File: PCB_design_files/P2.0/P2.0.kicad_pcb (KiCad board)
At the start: 4 copper layers, 19.8 x 10.9 mm, 31 parts, among them U1 INA819IDRGR

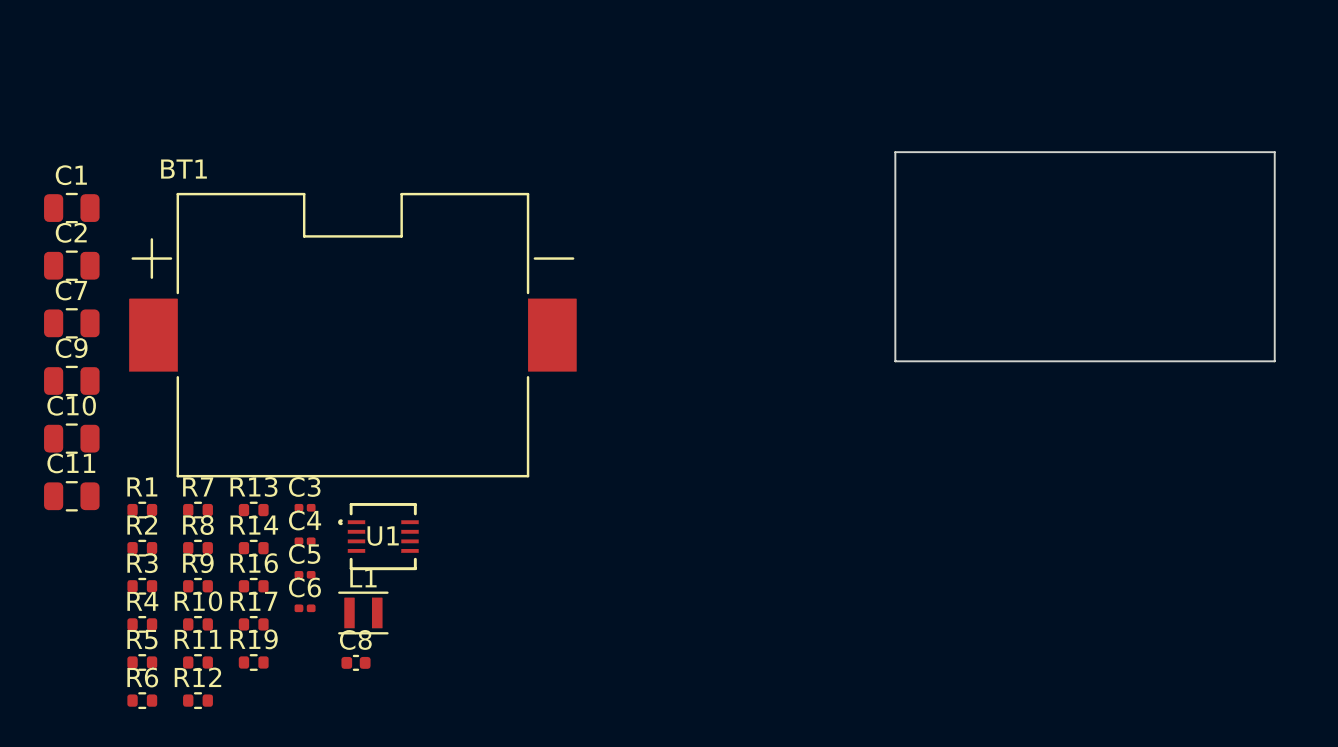
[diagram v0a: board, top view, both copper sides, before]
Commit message: PCB layout and component footprint updates
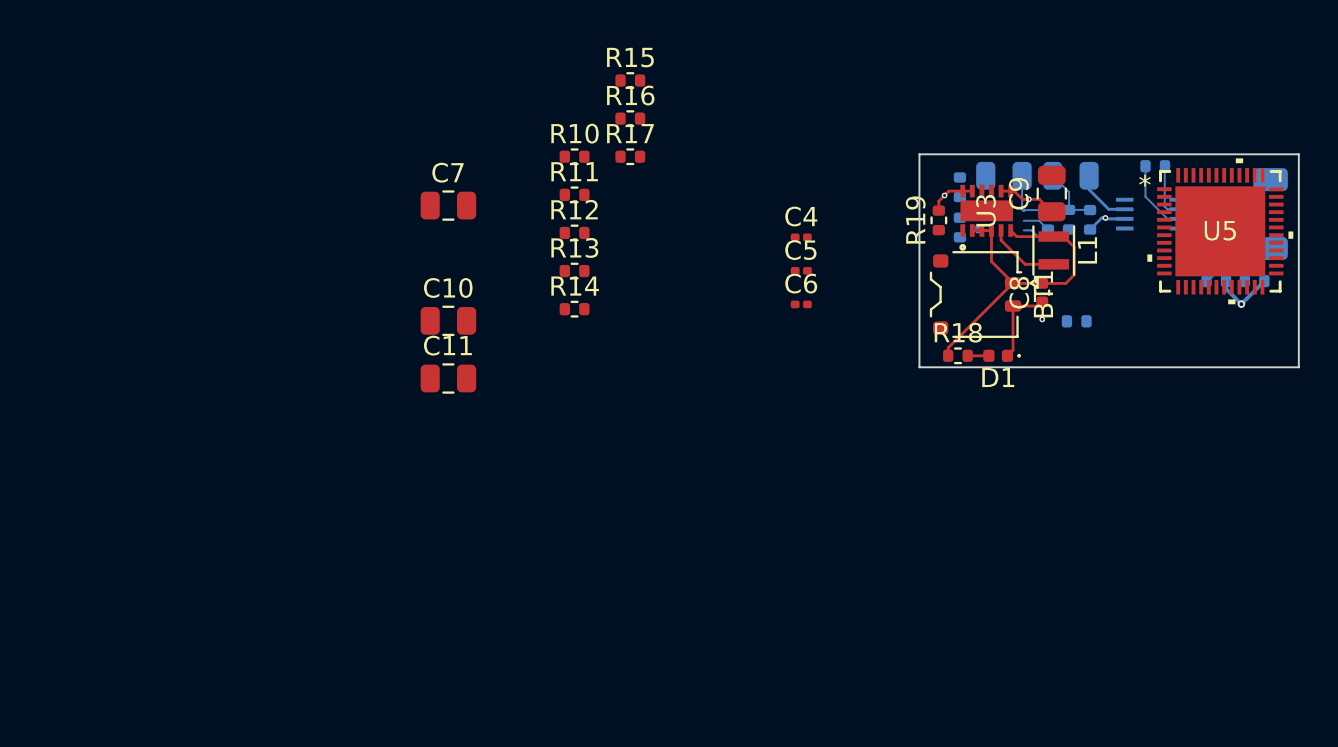
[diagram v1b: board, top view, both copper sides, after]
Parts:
- added D1: LED, LED_SMD:LED_0402_1005Metric, F.Cu at (80.3, 43.4)
- added J1: Conn_01x02_Pin, Connector_JST:JST_SH_BM02B-SRSS-TB_1x02-1MP_P1.00mm_Vertical, B.Cu at (93.3, 36.0)
- added R15: 100k, Resistor_SMD:R_0402_1005Metric, F.Cu at (61.1, 29.0)
- added R18: 1.1k, Resistor_SMD:R_0402_1005Metric, F.Cu at (78.2, 43.4)
- added U3: TPS61094, Library:TPS61094DSSR, F.Cu at (79.7, 35.8)
- added U5: NRF52832-QFAA-R, Library:QFN-48_NOR, F.Cu at (91.9, 36.9)
- BT1: footprint BHSD-1225-SM:BAT_BHSD-1225-SM -> Connector_JST:JST_ACH_BM02B-ACHSS-GAN-ETF_1x02-1MP_P1.20mm_Vertical
- C1, C2, C3, R1, R2, R3, R4, R5, R6, R7, R8, R9, U1: moved to B.Cu
- moved R1 59.3 mm to (93.7, 39.5)
- moved R2 57.8 mm to (91.7, 39.5)
- moved R3 57.3 mm to (88.5, 33.5), turned to 180 degrees
- moved R4 53.8 mm to (85.1, 36.3), turned to -90 degrees
- moved R5 53.6 mm to (84.0, 36.3), turned to -90 degrees
- moved R6 53.5 mm to (82.9, 36.3), turned to -90 degrees
- moved C1 52.2 mm to (84.1, 34.0), turned to 180 degrees
- moved C9 52.1 mm to (83.1, 34.9), turned to 90 degrees
- moved C2 48.9 mm to (80.6, 34.0), turned to 180 degrees
- moved R7 46.9 mm to (84.4, 41.6), turned to 180 degrees
- moved R9 44.9 mm to (78.3, 34.6), turned to -90 degrees
- moved U1 43.5 mm to (88.3, 36.0), turned to 180 degrees
- moved R8 43.2 mm to (78.3, 36.7), turned to -90 degrees
- moved R19 42.6 mm to (77.2, 36.3), turned to 90 degrees
- moved C8 40.7 mm to (82.6, 40.1), turned to 90 degrees
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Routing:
- net Net-(BT1-+): track 0.00 -> 17.9 mm
- net GND: track 0.00 -> 16.1 mm, vias 0 -> 5
- net /EEG+: track 0.00 -> 7.63 mm
- net /EEG-: track 0.00 -> 7.06 mm
- net Net-(R3-Pad2): track 0.00 -> 3.79 mm
- net Net-(U3-SW): track 0.00 -> 3.78 mm
- net Net-(C1-Pad2): track 0.00 -> 3.24 mm
- net Net-(U2-OUT1): track 0.00 -> 3.17 mm
- net Net-(U1-OUT): track 0.00 -> 3.01 mm
- net Net-(R3-Pad1): track 0.00 -> 2.88 mm
- net Net-(U2-IN1+): track 0.00 -> 2.78 mm
- net Net-(U2-IN1-): track 0.00 -> 1.45 mm
- net Net-(D1-A): track 0.00 -> 1.11 mm
- added copper zone on In2.Cu, net +3V3
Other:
- board size 19.8 x 10.9 mm -> 19.8 x 11.1 mm

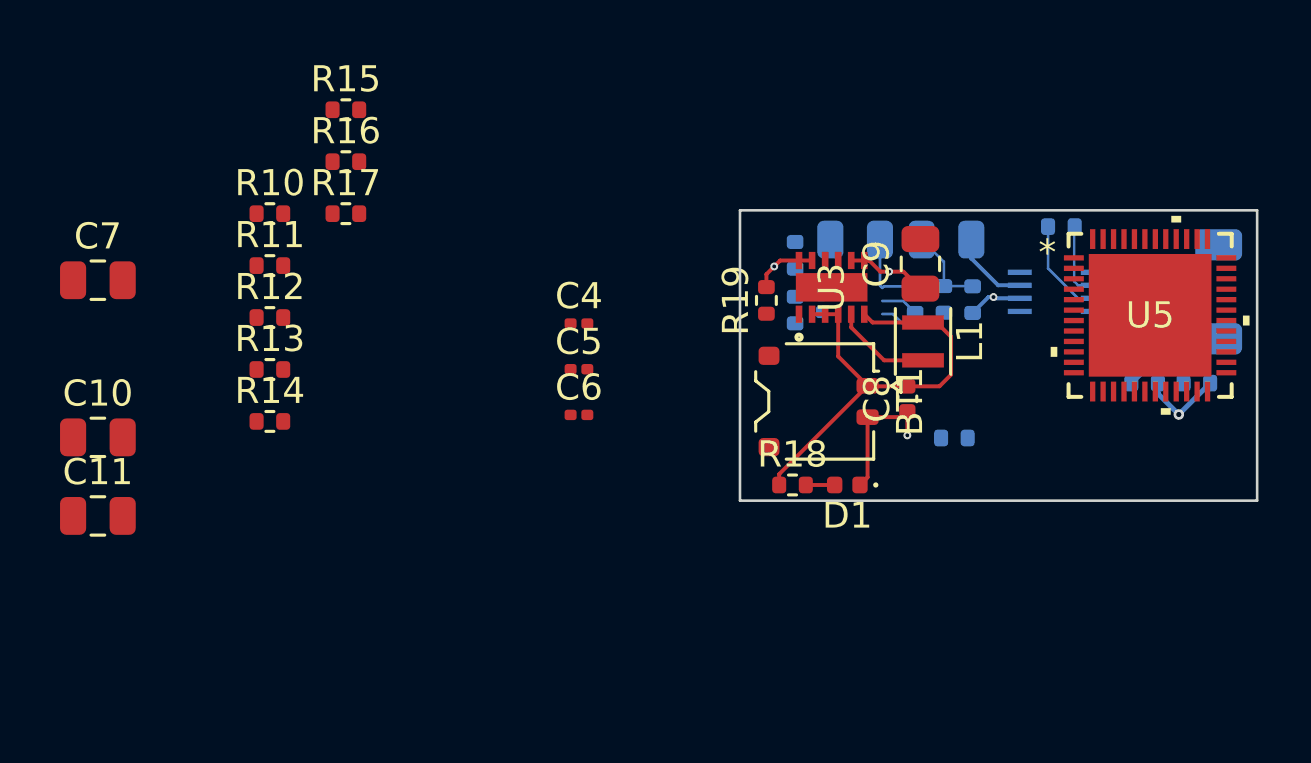
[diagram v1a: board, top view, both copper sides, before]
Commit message: Increased board size
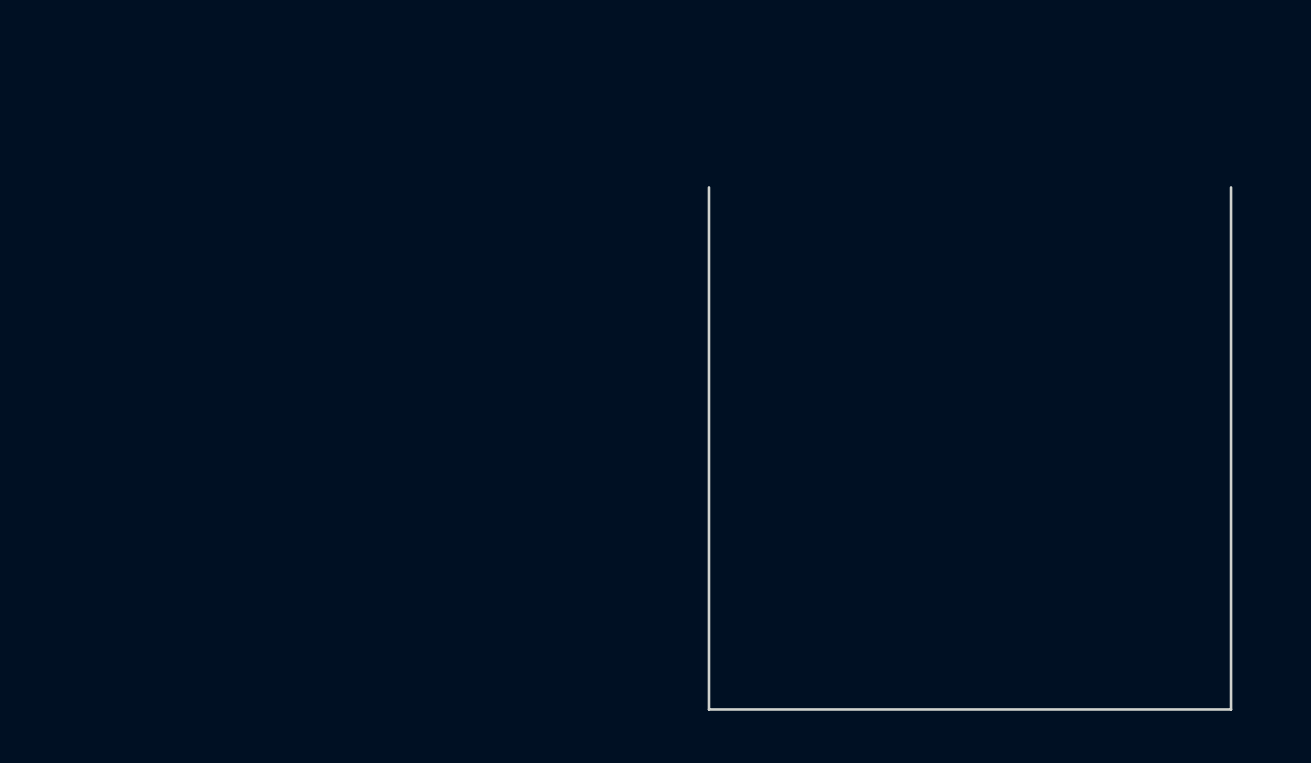
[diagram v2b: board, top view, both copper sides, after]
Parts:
- removed BT1: BHSD-1225-SM, Connector_JST:JST_ACH_BM02B-ACHSS-GAN-ETF_1x02-1MP_P1.20mm_Vertical
- removed C1, C10, C11, C2, C7: 10uF, Capacitor_SMD:C_0805_2012Metric
- removed C3, C4, C5: 0.1uF, Capacitor_SMD:C_0201_0603Metric
- removed C6: 10nF, Capacitor_SMD:C_0201_0603Metric
- removed C8: 2.2uF, Capacitor_SMD:C_0402_1005Metric
- removed C9: 33uF, Capacitor_SMD:C_0805_2012Metric
- removed D1: LED, LED_SMD:LED_0402_1005Metric
- removed J1: Conn_01x02_Pin, Connector_JST:JST_SH_BM02B-SRSS-TB_1x02-1MP_P1.00mm_Vertical
- removed L1: 2.2uH, Inductor_SMD:L_Murata_DFE201610P
- removed R1, R2: 68k, Resistor_SMD:R_0402_1005Metric
- removed R10: 604, Resistor_SMD:R_0402_1005Metric
- removed R11: 16k, Resistor_SMD:R_0402_1005Metric
- removed R12: 2.49k, Resistor_SMD:R_0402_1005Metric
- removed R13: 49.9k, Resistor_SMD:R_0402_1005Metric
- removed R14: 10k, Resistor_SMD:R_0402_1005Metric
- removed R15, R16, R4, R8, R9: 100k, Resistor_SMD:R_0402_1005Metric
- removed R17: ?150k, Resistor_SMD:R_0402_1005Metric
- removed R18, R19: 1.1k, Resistor_SMD:R_0402_1005Metric
- removed R3: 8.2k, Resistor_SMD:R_0402_1005Metric
- removed R5, R7: 1k, Resistor_SMD:R_0402_1005Metric
- removed R6: ?100k, Resistor_SMD:R_0402_1005Metric
- removed U1: INA819IDRGR, Library:SON_9IDRGR_TEX
- removed U3: TPS61094, Library:TPS61094DSSR
- removed U5: NRF52832-QFAA-R, Library:QFN-48_NOR
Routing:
- net Net-(BT1-+): track 17.9 -> 0.00 mm
- net GND: track 16.1 -> 0.00 mm, vias 5 -> 0
- net /EEG+: track 7.63 -> 0.00 mm
- net /EEG-: track 7.06 -> 0.00 mm
- net Net-(R3-Pad2): track 3.79 -> 0.00 mm
- net Net-(U3-SW): track 3.78 -> 0.00 mm
- net Net-(C1-Pad2): track 3.24 -> 0.00 mm
- net Net-(U2-OUT1): track 3.17 -> 0.00 mm
- net Net-(U1-OUT): track 3.01 -> 0.00 mm
- net Net-(R3-Pad1): track 2.88 -> 0.00 mm
- net Net-(U2-IN1+): track 2.78 -> 0.00 mm
- net Net-(U2-IN1-): track 1.45 -> 0.00 mm
- net Net-(D1-A): track 1.11 -> 0.00 mm
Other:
- board size 19.8 x 11.1 mm -> 20 x 20 mm

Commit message: Updated P2.0
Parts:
- added AE1: Antenna_Chip, Library:XDCR_2450AT18B100E, F.Cu at (76.2, 34.5)
- added BT1: BHSD-1225-SM, Connector_JST:JST_ACH_BM02B-ACHSS-GAN-ETF_1x02-1MP_P1.20mm_Vertical, F.Cu at (88.2, 45.1)
- added C1: 10uF, Capacitor_SMD:C_0805_2012Metric, B.Cu at (81.0, 38.5)
- added C10: 1uF, Capacitor_SMD:C_0805_2012Metric, B.Cu at (89.0, 47.5)
- added C11: 1uF, Capacitor_SMD:C_0805_2012Metric, B.Cu at (89.0, 45.2)
- added C12: 100nF, Capacitor_SMD:C_0402_1005Metric, F.Cu at (88.2, 39.0)
- added C13: 100nF, Capacitor_SMD:C_0402_1005Metric, F.Cu at (81.8, 41.0)
- added C14: 100nF, Capacitor_SMD:C_0402_1005Metric, F.Cu at (79.8, 41.0)
- added C15: 1.2pF, Capacitor_SMD:C_0402_1005Metric, F.Cu at (77.8, 39.5)
- added C16: 12pF, Capacitor_SMD:C_0402_1005Metric, F.Cu at (80.8, 41.0)
- added C17: 100pF, Capacitor_SMD:C_0402_1005Metric, F.Cu at (78.8, 41.0)
- added C18: 12pF, Capacitor_SMD:C_0402_1005Metric, F.Cu at (77.8, 41.0)
- added C19: 1uF, Capacitor_SMD:C_0603_1608Metric, F.Cu at (84.0, 41.0)
- added C2: 10uF, Capacitor_SMD:C_0805_2012Metric, B.Cu at (66.9, 35.2)
- added C20: 4.7uF, Capacitor_SMD:C_0603_1608Metric, F.Cu at (84.0, 42.8)
- added C21: N.C., Capacitor_SMD:C_0402_1005Metric, F.Cu at (78.5, 37.2)
- added C3: 0.1uF, Capacitor_SMD:C_0201_0603Metric, B.Cu at (54.3, 43.5)
- added C4: 0.1uF, Capacitor_SMD:C_0201_0603Metric, B.Cu at (54.3, 45.2)
- added C5: 0.1uF, Capacitor_SMD:C_0201_0603Metric, B.Cu at (54.3, 47.0)
- added C6: 10nF, Capacitor_SMD:C_0201_0603Metric, B.Cu at (54.3, 48.7)
- added C7: 10uF, Capacitor_SMD:C_0805_2012Metric, B.Cu at (66.9, 38.2)
- added C8: 2.2uF, Capacitor_SMD:C_0402_1005Metric, F.Cu at (89.8, 39.8)
- added C9: 33uF, Capacitor_SMD:C_0805_2012Metric, F.Cu at (79.8, 46.5)
- added D1: LED, LED_SMD:LED_0402_1005Metric, F.Cu at (89.8, 40.8)
- added J1: EEG_IN, Connector_JST:JST_SH_BM02B-SRSS-TB_1x02-1MP_P1.00mm_Vertical, B.Cu at (78.0, 46.4)
- added L1: 2.2uH, Inductor_SMD:L_Murata_DFE201610P, F.Cu at (80.3, 44.2)
- added L2: 3.3nH, Inductor_SMD:L_0402_1005Metric, F.Cu at (76.2, 38.0)
- added L3: 2.7nH, Inductor_SMD:L_0402_1005Metric, F.Cu at (76.2, 41.0)
- added R1: 68k, Resistor_SMD:R_0402_1005Metric, B.Cu at (79.0, 42.8)
- added R10: 604, Resistor_SMD:R_0402_1005Metric, B.Cu at (57.4, 41.6)
- added R11: 16k, Resistor_SMD:R_0402_1005Metric, B.Cu at (54.5, 31.7)
- added R12: 2.49k, Resistor_SMD:R_0402_1005Metric, B.Cu at (54.5, 33.7)
- added R13: 49.9k, Resistor_SMD:R_0402_1005Metric, B.Cu at (54.5, 35.7)
- added R14: 10k, Resistor_SMD:R_0402_1005Metric, B.Cu at (54.5, 37.6)
- added R15: 100k, Resistor_SMD:R_0402_1005Metric, B.Cu at (54.5, 39.6)
- added R16: 100k, Resistor_SMD:R_0402_1005Metric, B.Cu at (54.5, 41.6)
- added R17: ?150k, Resistor_SMD:R_0402_1005Metric, B.Cu at (51.6, 31.7)
- added R18: 1.1k, Resistor_SMD:R_0402_1005Metric, F.Cu at (89.8, 41.8)
- added R19: 1.1k, Resistor_SMD:R_0402_1005Metric, F.Cu at (89.8, 38.8)
- added R2: 68k, Resistor_SMD:R_0402_1005Metric, B.Cu at (77.0, 42.8)
- added R20: 10k, Resistor_SMD:R_0402_1005Metric, F.Cu at (88.2, 37.0)
- added R3: 8.2k, Resistor_SMD:R_0402_1005Metric, B.Cu at (78.0, 41.4)
- added R4: 100k, Resistor_SMD:R_0402_1005Metric, B.Cu at (80.8, 41.0)
- added R5: 1k, Resistor_SMD:R_0402_1005Metric, B.Cu at (80.7, 42.2)
- added R6: ?100k, Resistor_SMD:R_0402_1005Metric, B.Cu at (57.4, 33.7)
- added R7: 1k, Resistor_SMD:R_0402_1005Metric, B.Cu at (57.4, 35.7)
- added R8: 100k, Resistor_SMD:R_0402_1005Metric, B.Cu at (57.4, 37.6)
- added R9: 100k, Resistor_SMD:R_0402_1005Metric, B.Cu at (57.4, 39.6)
- added U1: INA819IDRGR, Library:SON_9IDRGR_TEX, B.Cu at (78.0, 38.6)
- added U3: TPS61094, Library:TPS61094DSSR, F.Cu at (83.8, 45.7)
- added U5: NRF52832-QFAA-R, Library:QFN-48_NOR, F.Cu at (83.0, 36.5)
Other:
- board size 20 x 20 mm -> 16 x 17 mm

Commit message: Updated schematic
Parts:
- removed AE1: Antenna_Chip, Library:XDCR_2450AT18B100E
- removed BT1: BHSD-1225-SM, Connector_JST:JST_ACH_BM02B-ACHSS-GAN-ETF_1x02-1MP_P1.20mm_Vertical
- removed C1, C2, C7: 10uF, Capacitor_SMD:C_0805_2012Metric
- removed C10, C11: 1uF, Capacitor_SMD:C_0805_2012Metric
- removed C12, C13, C14: 100nF, Capacitor_SMD:C_0402_1005Metric
- removed C15: 1.2pF, Capacitor_SMD:C_0402_1005Metric
- removed C16, C18: 12pF, Capacitor_SMD:C_0402_1005Metric
- removed C17: 100pF, Capacitor_SMD:C_0402_1005Metric
- removed C19: 1uF, Capacitor_SMD:C_0603_1608Metric
- removed C20: 4.7uF, Capacitor_SMD:C_0603_1608Metric
- removed C21: N.C., Capacitor_SMD:C_0402_1005Metric
- removed C3, C4, C5: 0.1uF, Capacitor_SMD:C_0201_0603Metric
- removed C6: 10nF, Capacitor_SMD:C_0201_0603Metric
- removed C8: 2.2uF, Capacitor_SMD:C_0402_1005Metric
- removed C9: 33uF, Capacitor_SMD:C_0805_2012Metric
- removed D1: LED, LED_SMD:LED_0402_1005Metric
- removed J1: EEG_IN, Connector_JST:JST_SH_BM02B-SRSS-TB_1x02-1MP_P1.00mm_Vertical
- removed L1: 2.2uH, Inductor_SMD:L_Murata_DFE201610P
- removed L2: 3.3nH, Inductor_SMD:L_0402_1005Metric
- removed L3: 2.7nH, Inductor_SMD:L_0402_1005Metric
- removed R1, R2: 68k, Resistor_SMD:R_0402_1005Metric
- removed R10: 604, Resistor_SMD:R_0402_1005Metric
- removed R11: 16k, Resistor_SMD:R_0402_1005Metric
- removed R12: 2.49k, Resistor_SMD:R_0402_1005Metric
- removed R13: 49.9k, Resistor_SMD:R_0402_1005Metric
- removed R14, R20: 10k, Resistor_SMD:R_0402_1005Metric
- removed R15, R16, R4, R8, R9: 100k, Resistor_SMD:R_0402_1005Metric
- removed R17: ?150k, Resistor_SMD:R_0402_1005Metric
- removed R18, R19: 1.1k, Resistor_SMD:R_0402_1005Metric
- removed R3: 8.2k, Resistor_SMD:R_0402_1005Metric
- removed R5, R7: 1k, Resistor_SMD:R_0402_1005Metric
- removed R6: ?100k, Resistor_SMD:R_0402_1005Metric
- removed U1: INA819IDRGR, Library:SON_9IDRGR_TEX
- removed U3: TPS61094, Library:TPS61094DSSR
- removed U5: NRF52832-QFAA-R, Library:QFN-48_NOR
